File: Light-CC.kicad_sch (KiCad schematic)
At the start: 17 parts, among them J1 Conn_01x02_Pin, J2 Conn_01x02_Pin, Q4 BS870, Q5 STD7NK40Z, U2 LM1117-3.3

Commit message: Done
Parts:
- added D2: SS14/SS34, Diode_SMD:D_SMA, symbol Diode:1N4007
- added J5: Conn_01x02_Pin, Connector_Wire:SolderWire-0.1sqmm_1x02_P3.6mm_D0.4mm_OD1mm_Relief, symbol Connector:Conn_01x02_Pin
- added Q7: BS870, Package_TO_SOT_SMD:SOT-23, symbol Transistor_FET:BS870
- added R2: 100K, symbol Device:R_US
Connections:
- net +3V3: now also D2.1 (K), J5.1 (Pin_1)
- net GND: now also Q7.2 (S), R2.2
- new net: D2.2 (A), J5.2 (Pin_2), Q7.3 (D)
- new net MCU/HAP_PWM: Q7.1 (G), R2.1
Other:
- sheet MCU ports: added HAP_PWM; removed none

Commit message: Added PolyFuse to output
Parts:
- added F5: Polyfuse, Fuse:Fuse_1206_3216Metric_Pad1.42x1.75mm_HandSolder, symbol Device:Polyfuse
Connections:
- net +12V: now also F5.1; no longer J2.1 (Pin_1)
- new net: F5.2, J2.1 (Pin_1)
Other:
- moved on the sheet: J2
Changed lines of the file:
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@@
   (junction (at 246.38 107.95) (diameter 0) (color 0 0 0 0)
   )
+  (junction (at 208.28 81.28) (diameter 0) (color 0 0 0 0)
+  )
+  (junction (at 217.17 81.28) (diameter 0) (color 0 0 0 0)
+  )
+  (junction (at 246.38 87.63) (diameter 0) (color 0 0 0 0)
+  )
+  (junction (at 36.83 163.83) (diameter 0) (color 0 0 0 0)
+  )
+  (junction (at 207.01 99.06) (diameter 0) (color 0 0 0 0)
+  )
+  (junction (at 66.04 66.04) (diameter 0) (color 0 0 0 0)
+  )
+  (junction (at 66.04 73.66) (diameter 0) (color 0 0 0 0)
+  )
+  (junction (at 57.15 163.83) (diameter 0) (color 0 0 0 0)
+  )
+  (junction (at 54.61 73.66) (diameter 0) (color 0 0 0 0)
+  )
   (junction (at 241.3 64.77) (diameter 0) (color 0 0 0 0)
   )
-  (junction (at 208.28 81.28) (diameter 0) (color 0 0 0 0)
-  )
-  (junction (at 217.17 81.28) (diameter 0) (color 0 0 0 0)
-  )
-  (junction (at 246.38 87.63) (diameter 0) (color 0 0 0 0)
-  )
-  (junction (at 36.83 163.83) (diameter 0) (color 0 0 0 0)
-  )
-  (junction (at 207.01 99.06) (diameter 0) (color 0 0 0 0)
-  )
-  (junction (at 66.04 66.04) (diameter 0) (color 0 0 0 0)
-  )
-  (junction (at 66.04 73.66) (diameter 0) (color 0 0 0 0)
-  )
-  (junction (at 57.15 163.83) (diameter 0) (color 0 0 0 0)
-  )
-  (junction (at 54.61 73.66) (diameter 0) (color 0 0 0 0)
-  )
   (junction (at 173.99 125.73) (diameter 0) (color 0 0 0 0)
   )
@@
     (stroke (width 0) (type default))
   )
+  (wire (pts (xy 252.73 64.77) (xy 254 64.77))
+    (stroke (width 0) (type default))
+  )
   (wire (pts (xy 173.99 118.11) (xy 167.64 118.11))
     (stroke (width 0) (type default))
@@
     (stroke (width 0) (type default))
   )
+  (wire (pts (xy 241.3 64.77) (xy 245.11 64.77))
+    (stroke (width 0) (type default))
+  )
   (wire (pts (xy 246.38 81.28) (xy 246.38 77.47))
     (stroke (width 0) (type default))
@@
     (stroke (width 0) (type default))
   )
-  (wire (pts (xy 241.3 64.77) (xy 248.92 64.77))
-    (stroke (width 0) (type default))
-  )
   (wire (pts (xy 157.48 144.78) (xy 173.99 144.78))
     (stroke (width 0) (type default))
@@
     (stroke (width 0) (type default))
   )
-  (wire (pts (xy 246.38 67.31) (xy 248.92 67.31))
+  (wire (pts (xy 246.38 67.31) (xy 254 67.31))
     (stroke (width 0) (type default))
   )
@@
     )
   )
+  (symbol (lib_id "Device:Polyfuse") (at 248.92 64.77 90) (unit 1)
+    (in_bom yes) (on_board yes) (dnp no)
+    (property "Reference" "F5" (at 242.57 62.23 90)
+      (effects (font (size 1.27 1.27)) (justify left))
+    )
+    (property "Value" "Polyfuse" (at 251.46 62.23 90)
+      (effects (font (size 1.27 1.27)) (justify left))
+    )
+    (property "Footprint" "Fuse:Fuse_1206_3216Metric_Pad1.42x1.75mm_HandSolder" (at 254 63.5 0)
+      (effects (font (size 1.27 1.27)) (justify left) hide)
+    )
+    (property "Datasheet" "~" (at 248.92 64.77 0)
+      (effects (font (size 1.27 1.27)) hide)
+    )
+    (pin "1")
+    (pin "2")
+    (instances
+      (project "V4_DO"
+        (path "/3276f334-7f44-4257-9227-3addac41659f"
+          (reference "F5") (unit 1)
+        )
+      )
+      (project "Light-CC"
+        (path "/a3254443-8240-44f0-af35-274db02f779b"
+          (reference "F1") (unit 1)
+        )
+      )
+      (project "V4_DO_LowSide"
+        (path "/d7f1bed0-d765-402e-9acc-bf190c5e1715"
+          (reference "F5") (unit 1)
+        )
+      )
+    )
+  )
   (symbol (lib_id "power:GND") (at 57.15 170.18 0) (unit 1)
     (in_bom yes) (on_board yes) (dnp no) (fields_autoplaced)
@@
     )
   )
-  (symbol (lib_id "Connector:Conn_01x02_Pin") (at 254 64.77 0) (mirror y) (unit 1)
-    (in_bom yes) (on_board yes) (dnp no) (fields_autoplaced)
-    (property "Reference" "J2" (at 255.27 64.77 0)
+  (symbol (lib_id "Connector:Conn_01x02_Pin") (at 259.08 64.77 0) (mirror y) (unit 1)
+    (in_bom yes) (on_board yes) (dnp no) (fields_autoplaced)
+    (property "Reference" "J2" (at 260.35 64.77 0)
       (effects (font (size 1.27 1.27)) (justify right))
     )
-    (property "Value" "Conn_01x02_Pin" (at 255.27 67.31 0)
+    (property "Value" "Conn_01x02_Pin" (at 260.35 67.31 0)
       (effects (font (size 1.27 1.27)) (justify right))
     )
-    (property "Footprint" "Connector_Wire:SolderWire-0.75sqmm_1x02_P7mm_D1.25mm_OD3.5mm" (at 254 64.77 0)
-      (effects (font (size 1.27 1.27)) hide)
-    )
-    (property "Datasheet" "~" (at 254 64.77 0)
-      (effects (font (size 1.27 1.27)) hide)
-    )
+    (property "Footprint" "Connector_Wire:SolderWire-0.75sqmm_1x02_P7mm_D1.25mm_OD3.5mm" (at 259.08 64.77 0)
+      (effects (font (size 1.27 1.27)) hide)
+    )
+    (property "Datasheet" "~" (at 259.08 64.77 0)
+      (effects (font (size 1.27 1.27)) hide)
+    )

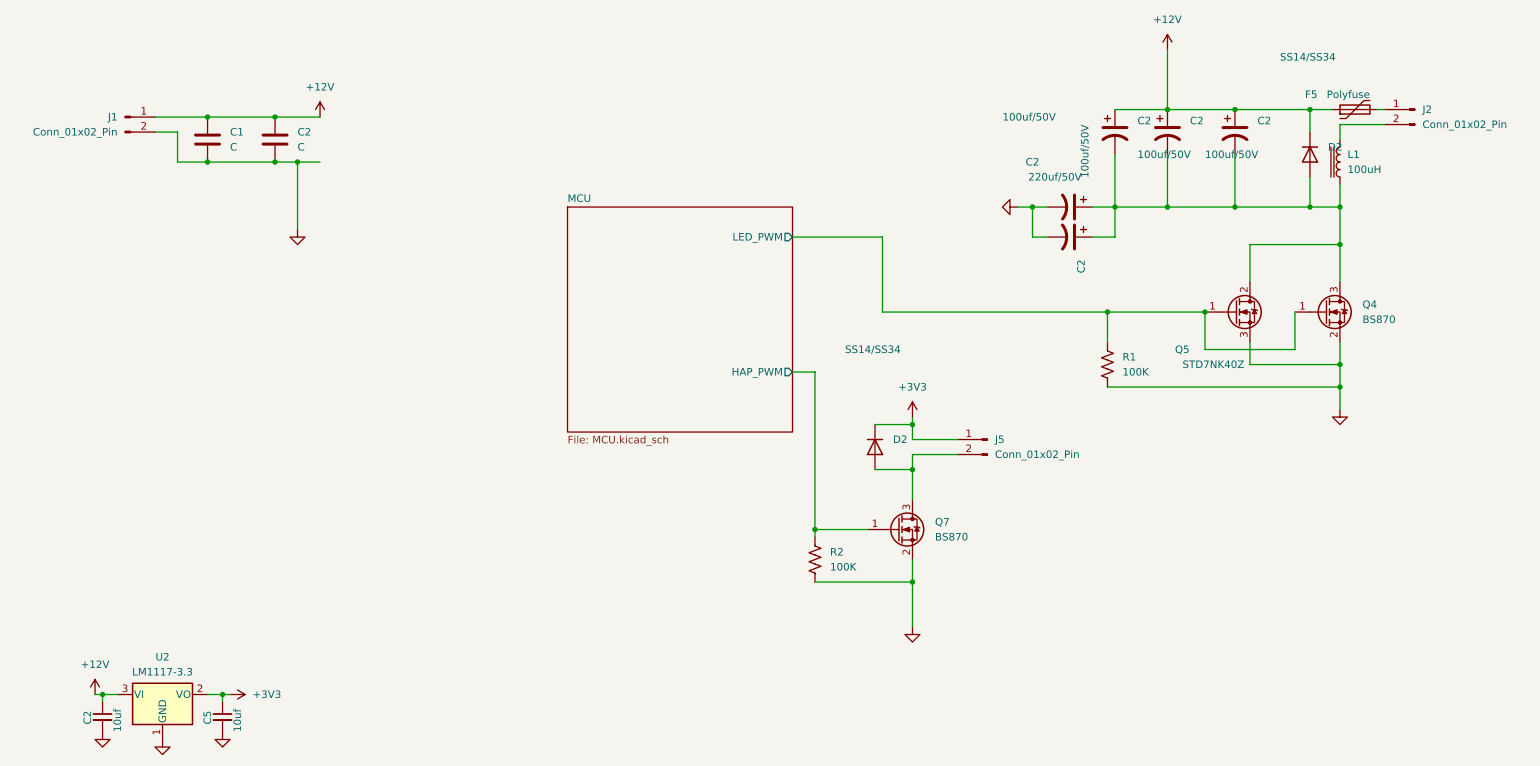
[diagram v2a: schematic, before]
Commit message: Changed the layout based on Power supply
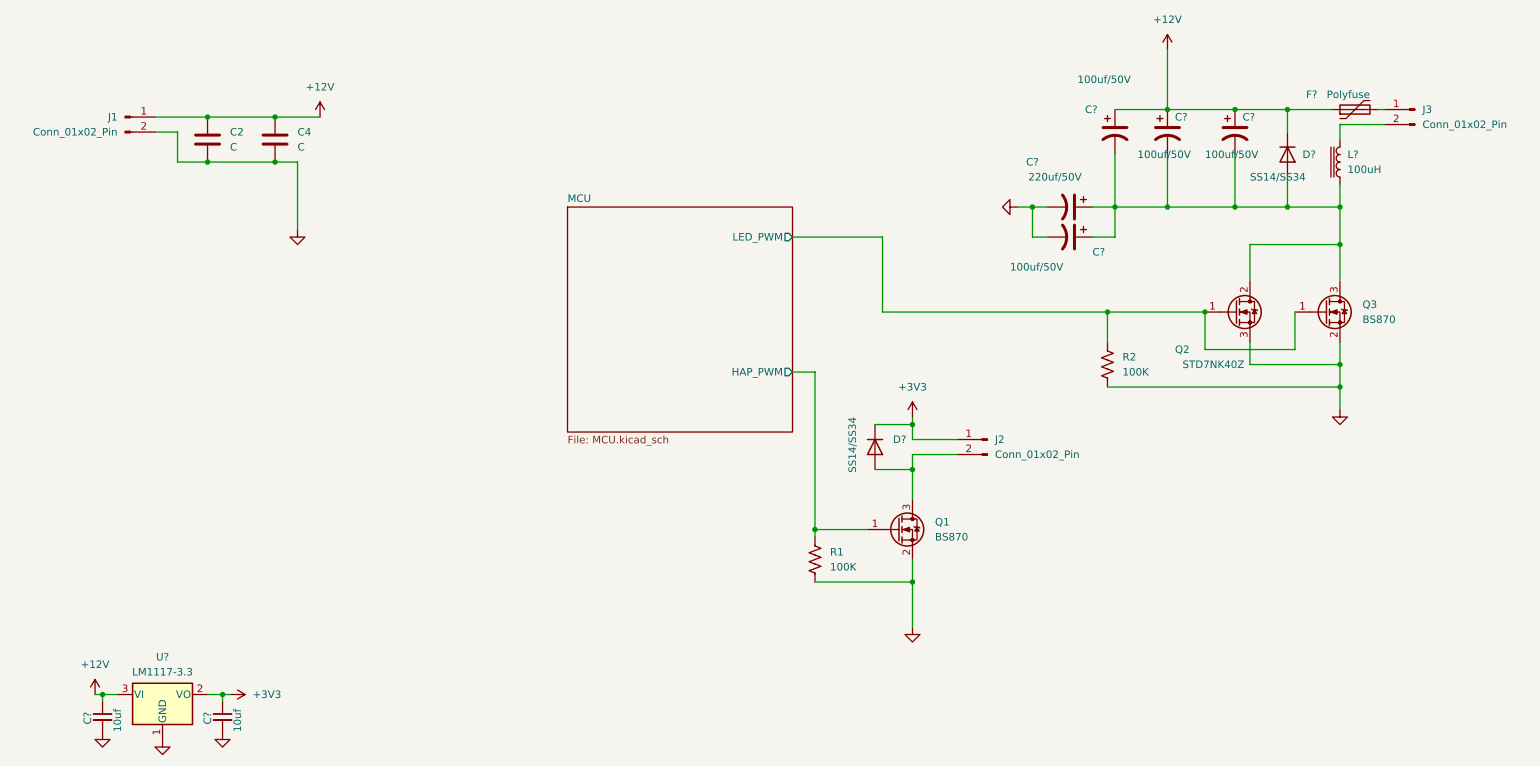
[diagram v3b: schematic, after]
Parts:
- C2: renamed from C1; footprint Capacitor_SMD:C_0805_2012Metric_Pad1.18x1.45mm_HandSolder -> Capacitor_SMD:C_0805_2012Metric
- C4: renamed from C2; footprint Capacitor_SMD:C_0805_2012Metric_Pad1.18x1.45mm_HandSolder -> Capacitor_SMD:C_0805_2012Metric
- C? (x5): renamed from C2; footprint Capacitor_SMD:C_1206_3216Metric_Pad1.33x1.80mm_HandSolder -> Capacitor_SMD:C_1206_3216Metric
- F?: renamed from F5; footprint Fuse:Fuse_1206_3216Metric_Pad1.42x1.75mm_HandSolder -> Fuse:Fuse_1206_3216Metric
- R1: renamed from R2; footprint (none) -> Resistor_SMD:R_0805_2012Metric
- R2: renamed from R1; footprint (none) -> Resistor_SMD:R_0805_2012Metric
- renumbered C2 to C?, C5 to C?, D2 to D?, J5 to J2, J2 to J3, L1 to L?, Q7 to Q1, Q5 to Q2, Q4 to Q3, U2 to U?
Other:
- moved on the sheet: D?

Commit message: Layout Routing is 50% complete
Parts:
- C? (x2): footprint Capacitor_SMD:C_1206_3216Metric -> Capacitor_THT:CP_Radial_D5.0mm_P2.50mm
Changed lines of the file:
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@@
       (effects (font (size 1.27 1.27)) (justify left))
     )
-    (property "Footprint" "Capacitor_SMD:C_1206_3216Metric" (at 208.28 68.58 0)
+    (property "Footprint" "Capacitor_THT:CP_Radial_D5.0mm_P2.50mm" (at 208.28 68.58 0)
       (effects (font (size 1.27 1.27)) hide)
     )
@@
       (effects (font (size 1.27 1.27)) (justify left))
     )
-    (property "Footprint" "Capacitor_SMD:C_1206_3216Metric" (at 217.17 68.58 0)
+    (property "Footprint" "Capacitor_THT:CP_Radial_D5.0mm_P2.50mm" (at 217.17 68.58 0)
       (effects (font (size 1.27 1.27)) hide)
     )

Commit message: Layout & routing is almost done Logo need to added
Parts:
- J2: footprint Connector_Wire:SolderWire-0.1sqmm_1x02_P3.6mm_D0.4mm_OD1mm_Relief -> Connector_Wire:SolderWire-0.75sqmm_1x02_P4.8mm_D1.25mm_OD2.3mm_Relief
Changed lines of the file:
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@@
       (effects (font (size 1.27 1.27)) (justify right))
     )
-    (property "Footprint" "Connector_Wire:SolderWire-0.1sqmm_1x02_P3.6mm_D0.4mm_OD1mm_Relief" (at 186.69 120.65 0)
+    (property "Footprint" "Connector_Wire:SolderWire-0.75sqmm_1x02_P4.8mm_D1.25mm_OD2.3mm_Relief" (at 186.69 120.65 0)
       (effects (font (size 1.27 1.27)) hide)
     )
